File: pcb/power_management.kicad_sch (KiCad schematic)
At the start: 34 parts, among them J3 USB C, J4 BATT, Q2 AO3400A, Q3 AO3401A, SW5 POWER, U4 BQ25619, U5 AP2112K-3.3

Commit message: perf: strenghen Mahony filter (#50)
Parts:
- U5: footprint leany_footprints:TSOT-23-5 -> Package_TO_SOT_SMD:SOT-23-5
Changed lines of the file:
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@@
 (kicad_sch
-	(version 20231120)
+	(version 20250114)
 	(generator "eeschema")
-	(generator_version "8.0")
+	(generator_version "9.0")
 	(paper "A4")
 	(title_block
@@
 		(comment 2 "Copyright (c) 2023 Gilles Henrard")
 	)
+	(rectangle
+		(start 208.28 26.67)
+		(end 261.62 60.96)
+		(stroke
+			(width 0)
+			(type dash)
+		)
+		(fill
+			(type none)
+		)
+	)
+	(rectangle
+		(start 109.22 25.4)
+		(end 198.628 88.9)
+		(stroke
+			(width 0)
+			(type dash)
+		)
+		(fill
+			(type none)
+		)
+	)
+	(rectangle
+		(start 36.83 115.57)
+		(end 100.33 170.18)
+		(stroke
+			(width 0)
+			(type dash)
+		)
+		(fill
+			(type none)
+		)
+	)
+	(rectangle
+		(start 40.64 27.94)
+		(end 95.25 86.36)
+		(stroke
+			(width 0)
+			(type dash)
+		)
+		(fill
+			(type none)
+		)
+	)
+	(text "USB C connector (5V receiver)"
+		(exclude_from_sim no)
+		(at 62.484 84.836 0)
+		(effects
+			(font
+				(size 1.27 1.27)
+			)
+		)
+	)
+	(text "Battery voltage ADC measure point"
+		(exclude_from_sim no)
+		(at 55.118 165.608 0)
+		(effects
+			(font
+				(size 1.27 1.27)
+			)
+		)
+	)
+	(text "Highest input voltage regulation to 3.3V"
+		(exclude_from_sim no)
+		(at 235.458 57.15 0)
+		(effects
+			(font
+				(size 1.27 1.27)
+			)
+		)
+	)
+	(text "Avoids draining the battery when not reading its voltage"
+		(exclude_from_sim no)
+		(at 65.532 168.148 0)
+		(effects
+			(font
+				(size 1.27 1.27)
+			)
+		)
+	)
 	(junction
 		(at 166.37 53.34)
@@
 		)
 	)
-	(rectangle
-		(start 208.28 26.67)
-		(end 261.62 60.96)
-		(stroke
-			(width 0)
-			(type dash)
-		)
-		(fill
-			(type none)
-		)
-	)
-	(rectangle
-		(start 109.22 25.4)
-		(end 198.628 88.9)
-		(stroke
-			(width 0)
-			(type dash)
-		)
-		(fill
-			(type none)
-		)
-	)
-	(rectangle
-		(start 36.83 115.57)
-		(end 100.33 170.18)
-		(stroke
-			(width 0)
-			(type dash)
-		)
-		(fill
-			(type none)
-		)
-	)
-	(rectangle
-		(start 40.64 27.94)
-		(end 95.25 86.36)
-		(stroke
-			(width 0)
-			(type dash)
-		)
-		(fill
-			(type none)
-		)
-	)
-	(text "USB C connector (5V receiver)"
-		(exclude_from_sim no)
-		(at 62.484 84.836 0)
-		(effects
-			(font
-				(size 1.27 1.27)
-			)
-		)
-	)
-	(text "Battery voltage ADC measure point"
-		(exclude_from_sim no)
-		(at 55.118 165.608 0)
-		(effects
-			(font
-				(size 1.27 1.27)
-			)
-		)
-	)
-	(text "Highest input voltage regulation to 3.3V"
-		(exclude_from_sim no)
-		(at 235.458 57.15 0)
-		(effects
-			(font
-				(size 1.27 1.27)
-			)
-		)
-	)
-	(text "Avoids draining the battery when not reading its voltage"
-		(exclude_from_sim no)
-		(at 65.532 168.148 0)
-		(effects
-			(font
-				(size 1.27 1.27)
-			)
-		)
-	)
 	(global_label "BATT_VOLT"
 		(shape output)
@@
 			)
 		)
-		(property "Footprint" "leany_footprints:TSOT-23-5"
+		(property "Footprint" "Package_TO_SOT_SMD:SOT-23-5"
 			(at 237.49 31.115 0)
 			(effects

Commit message: feat: design PCB rev0.3 (#27)
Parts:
- removed J4: BATT, leany_footprints:wago_2060-452_998-404, symbol leany-symbols:wago_2060-452_998-404
- added C28: 100n, leany_footprints:C_0402_1005Metric, symbol Device:C_Small
- added J4: BATT, leany_footprints:wago_2059-302_998-403, symbol leany-symbols:wago_2059-302_998-403
- added Q4: AO3401A, Package_TO_SOT_SMD:SOT-23, symbol Transistor_FET:AO3401A
- added Q5: PT8810, Package_TO_SOT_SMD:SOT-23-6, symbol leany-symbols:PT8810
- added R25: 100R, leany_footprints:R_0402_1005Metric, symbol Device:R_Small
- added R26: 1k, leany_footprints:R_0402_1005Metric, symbol Device:R_Small
- added TP5: +BATT, leany_footprints:TestPoint_Pad_1.0x1.0mm, symbol Connector:TestPoint_Small
- added U6: DW01A, Package_TO_SOT_SMD:SOT-23-6, symbol Battery_Management:DW01A
- C14, C22, C23: footprint Capacitor_SMD:C_0603_1608Metric -> leany_footprints:C_0402_1005Metric; LCSC C15849 -> C52923
- C17, C21: footprint Capacitor_SMD:C_0603_1608Metric -> leany_footprints:C_0402_1005Metric; LCSC C14663 -> C1525
- C20: footprint Capacitor_SMD:C_0603_1608Metric -> leany_footprints:C_0402_1005Metric; LCSC C21122 -> C1532
- J3: footprint Connector_USB:USB_C_Receptacle_HRO_TYPE-C-31-M-12 -> leany_footprints:USB_C_Receptacle_HRO_TYPE-C-31-M-12
- R16, R18: footprint Resistor_SMD:R_0603_1608Metric -> leany_footprints:R_0402_1005Metric; LCSC C25804 -> C25744
- R17: footprint Resistor_SMD:R_0603_1608Metric -> leany_footprints:R_0402_1005Metric; LCSC C25803 -> C25741
- R19, R20: footprint Resistor_SMD:R_0603_1608Metric -> leany_footprints:R_0402_1005Metric; LCSC C23186 -> C25905
- R23, R24: footprint Resistor_SMD:R_0603_1608Metric -> leany_footprints:R_0402_1005Metric; LCSC C23162 -> C25900
- renumbered TP1 to TP2, TP2 to TP3, TP3 to TP4, TP4 to TP6, TP5 to TP7
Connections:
- net +BATT: now also Q4.2 (S), R25.2
- net GND: now also Q5.3 (S2), R26.1
- new net: J4.1 (1_1), J4.2 (1_2), Q4.3 (D), TP5.1
- new net: C28.1, R25.1, U6.5 (VCC)
- new net: Q5.6 (G1), U6.1 (OD)
- new net: R26.2, U6.2 (CS)
- new net: Q5.4 (G2), U6.3 (OC)
- new net: Q5.2 (S1/D2), Q5.5 (S1/D2)
- new net GNDREF: C28.2, J4.3 (2_1), J4.4 (2_2), Q4.1 (G), Q5.1 (D1), U6.6 (GND)
- no-connect marks 6 -> 7
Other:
- note added: "Battery levels and reverse-voltage protection"
- title: Leany power management -> Leany - Power management
- moved on the sheet: C19, C20, C21, C22, C23, C24, TP6, TP7, U5

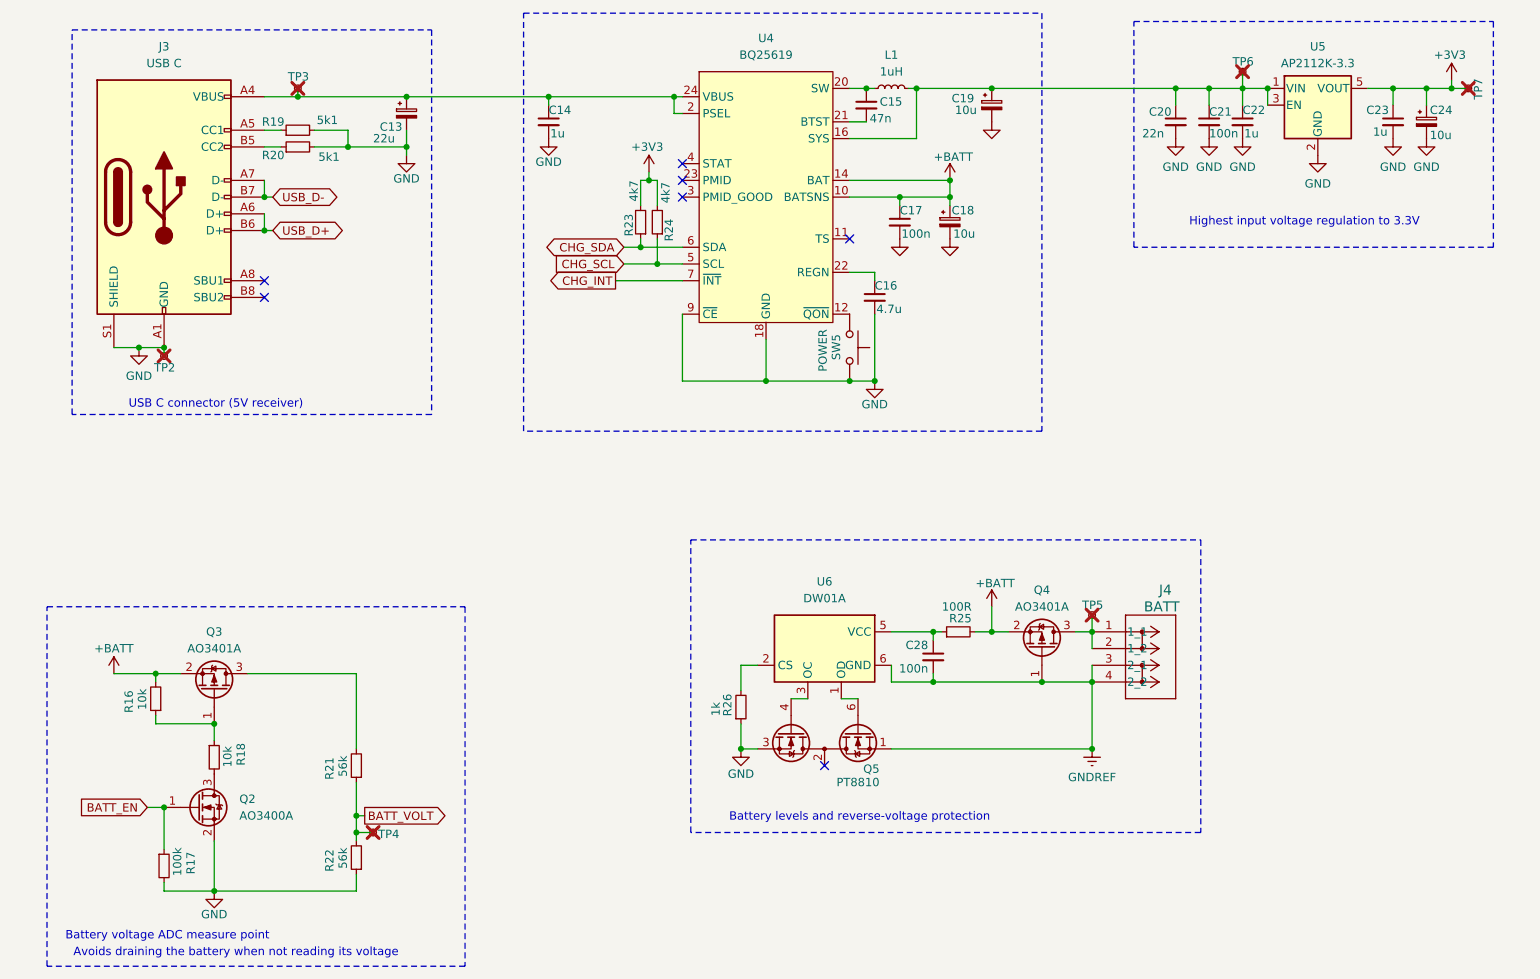
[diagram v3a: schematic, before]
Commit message: refactor: design PCB rev0.4 and fix validation workflow (#64)
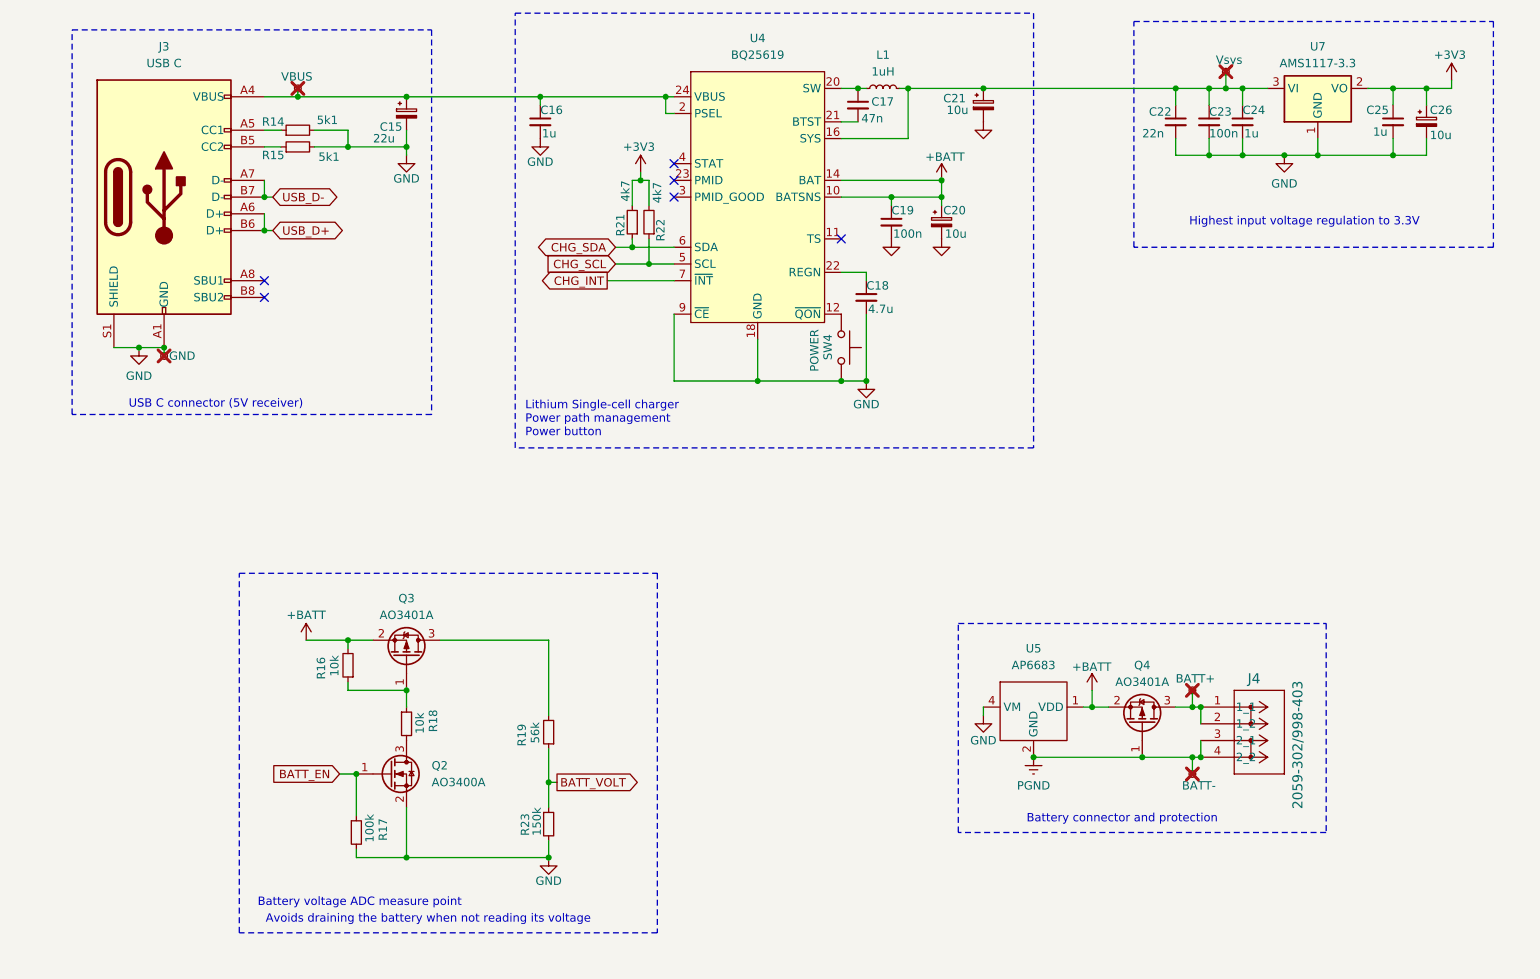
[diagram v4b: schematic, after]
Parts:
- removed C14: 1u, leany_footprints:C_0402_1005Metric, symbol Device:C_Small
- removed C15: 47n, Capacitor_SMD:C_0603_1608Metric, symbol Device:C_Small
- removed C28: 100n, leany_footprints:C_0402_1005Metric, symbol Device:C_Small
- removed Q5: PT8810, Package_TO_SOT_SMD:SOT-23-6, symbol leany-symbols:PT8810
- removed R24: 4k7, leany_footprints:R_0402_1005Metric, symbol Device:R_Small
- removed R25: 100R, leany_footprints:R_0402_1005Metric, symbol Device:R_Small
- removed R26: 1k, leany_footprints:R_0402_1005Metric, symbol Device:R_Small
- removed TP4: BATT, leany_footprints:TestPoint_Pad_1.0x1.0mm, symbol Connector:TestPoint_Small
- removed TP7: 3.3V, leany_footprints:TestPoint_Pad_1.0x1.0mm, symbol Connector:TestPoint_Small
- removed U5: AP2112K-3.3, Package_TO_SOT_SMD:SOT-23-5, symbol Regulator_Linear:AP2112K-3.3
- removed U6: DW01A, Package_TO_SOT_SMD:SOT-23-6, symbol Battery_Management:DW01A
- added C17: 47n, Capacitor_SMD:C_0603_1608Metric, symbol Device:C_Small
- added C18: 4.7u, Capacitor_SMD:C_0805_2012Metric, symbol Device:C_Small
- added R21: 4k7, leany_footprints:R_0402_1005Metric, symbol Device:R_Small
- added TP6: BATT-, leany_footprints:TestPoint_Pad_1.0x1.0mm, symbol Connector:TestPoint_Small
- added U5: AP6683, Package_DFN_QFN:UDFN-4-1EP_1x1mm_P0.65mm_EP0.48x0.48mm, symbol leany-symbols:AP6683
- added U7: AMS1117-3.3, Package_TO_SOT_SMD:SOT-223-3_TabPin2, symbol Regulator_Linear:AMS1117-3.3
- C16: value 4.7u -> 1u; footprint Capacitor_SMD:C_0805_2012Metric -> leany_footprints:C_0402_1005Metric; LCSC C1779 -> C52923
- J3: LCSC C136423 -> C2765186
- J4: value BATT -> 2059-302/998-403
- R22: value 56k -> 4k7; footprint Resistor_SMD:R_0603_1608Metric -> leany_footprints:R_0402_1005Metric; LCSC C23206 -> C25900
- R23: value 4k7 -> 150k; footprint leany_footprints:R_0402_1005Metric -> Resistor_SMD:R_0603_1608Metric; LCSC C25900 -> C22807
- TP5: value +BATT -> BATT+
- TP7: renamed from TP6; value Vin -> Vsys
- renumbered C13 to C15, C17 to C19, C18 to C20, C19 to C21, C20 to C22, C21 to C23, C22 to C24, C23 to C25, C24 to C26, R19 to R14, R20 to R15, R21 to R19, SW5 to SW4
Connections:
- net +3V3: now also R22.2, R21.2, U7.2 (VO); no longer R23.2
- net +BATT: now also U5.1 (VDD)
- net BATT_VOLT: now also R23.1; no longer R22.2
- net CHG_SCL: now also R22.1
- net CHG_SDA: now also R21.1; no longer R23.1
- net GND: now also R23.2, C18.2, U5.4 (VM), U5.5 (PAD), U7.1 (GND); no longer R22.1
- net at L1.1, U4.19 (SW), U4.20 (SW): now also C17.1
- net at C15.1, J3.A4 (VBUS), J3.A9 (VBUS)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: now also C16.1
- net at U4.21 (BTST): now also C17.2
- net at U4.22 (REGN): now also C18.1; no longer C16.1
- net GNDREF renamed PGND
- net PGND: now also TP6.1, U5.2 (GND), U5.3 (GND)
- net SYS: no longer names the net of C21.1, C22.1, C23.1, C24.1, L1.2, TP7.1, U4.15 (SYS), U4.16 (SYS)
- net SYS: now also U7.3 (VI)
- no-connect marks 7 -> 6
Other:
- note added: "Battery connector and protection"
- note added: "Lithium Single-cell charger Power path management Power button"
- note removed: "Battery levels and reverse-voltage protection"
- moved on the sheet: C19, C20, C21, L1, Q2, Q3, R16, R17, R18, R19, SW4

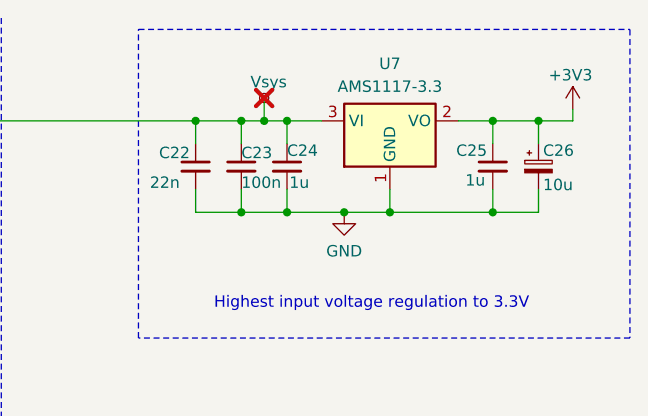
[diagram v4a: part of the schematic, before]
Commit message: fix: replace the LDO by an AP2112k-3.3 (#93)
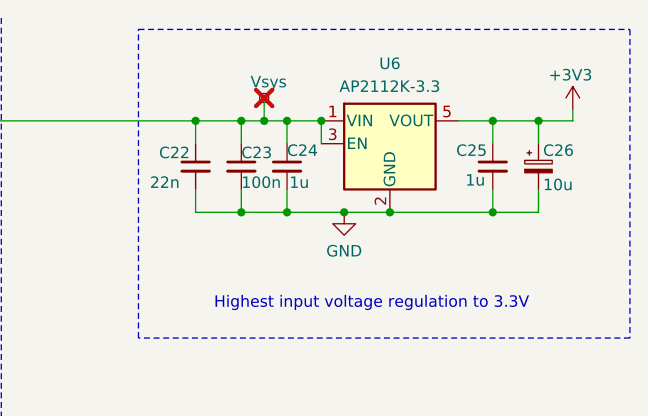
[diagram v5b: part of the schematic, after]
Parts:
- removed U7: AMS1117-3.3, Package_TO_SOT_SMD:SOT-223-3_TabPin2, symbol Regulator_Linear:AMS1117-3.3
- added U6: AP2112K-3.3, Package_TO_SOT_SMD:SOT-23-5, symbol Regulator_Linear:AP2112K-3.3
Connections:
- net +3V3: now also U6.5 (VOUT)
- net GND: now also U6.2 (GND)
- net at C21.1, C22.1, C23.1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: now also U6.1 (VIN), U6.3 (EN)
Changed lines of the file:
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@@
 	(title_block
 		(title "Leany - Power management")
-		(date "2026-02-19")
+		(date "2026-03-22")
 		(rev "0.4")
 		(comment 1 "CERN Open Hardware Licence Version 2 - Permissive")
@@
 	)
 	(junction
-		(at 229.87 46.99)
-		(diameter 0)
-		(color 0 0 0 0)
-	)
-	(junction
 		(at 172.72 53.34)
 		(diameter 0)
@@
 	)
 	(junction
+		(at 222.25 36.83)
+		(diameter 0)
+		(color 0 0 0 0)
+	)
+	(junction
 		(at 241.3 46.99)
 		(diameter 0)
@@
 	)
 	(junction
+		(at 229.87 46.99)
+		(diameter 0)
+		(color 0 0 0 0)
+	)
+	(junction
 		(at 241.3 36.83)
 		(diameter 0)
@@
 	(wire
 		(pts
+			(xy 229.87 46.99) (xy 241.3 46.99)
+		)
+		(stroke
+			(width 0)
+			(type default)
+		)
+	)
+	(wire
+		(pts
 			(xy 113.03 151.13) (xy 113.03 153.67)
 		)
@@
 	(wire
 		(pts
-			(xy 179.07 36.83) (xy 208.28 36.83)
+			(xy 222.25 39.37) (xy 222.25 36.83)
 		)
 		(stroke
@@
 	(wire
 		(pts
-			(xy 127 49.53) (xy 127 50.8)
+			(xy 179.07 36.83) (xy 208.28 36.83)
 		)
 		(stroke
@@
 	(wire
 		(pts
-			(xy 229.87 44.45) (xy 229.87 46.99)
+			(xy 127 49.53) (xy 127 50.8)
 		)
 		(stroke
@@
 	(wire
 		(pts
-			(xy 241.3 46.99) (xy 229.87 46.99)
+			(xy 224.79 46.99) (xy 229.87 46.99)
 		)
 		(stroke
@@
 	(wire
 		(pts
-			(xy 224.79 46.99) (xy 229.87 46.99)
-		)
-		(stroke
-			(width 0)
-			(type default)
-		)
-	)
-	(wire
-		(pts
 			(xy 46.99 76.2) (xy 50.8 76.2)
 		)
@@
 	)
 	(symbol
+		(lib_id "Regulator_Linear:AP2112K-3.3")
+		(at 229.87 39.37 0)
+		(unit 1)
+		(exclude_from_sim no)
+		(in_bom yes)
+		(on_board yes)
+		(dnp no)
+		(fields_autoplaced yes)
+		(property "Reference" "U6"
+			(at 229.87 30.48 0)
+			(effects
+				(font
+					(size 1.27 1.27)
+				)
+			)
+		)
+		(property "Value" "AP2112K-3.3"
+			(at 229.87 33.02 0)
+			(effects
+				(font
+					(size 1.27 1.27)
+				)
+			)
+		)
+		(property "Footprint" "Package_TO_SOT_SMD:SOT-23-5"
+			(at 229.87 31.115 0)
+			(effects
+				(font
+					(size 1.27 1.27)
+				)
+				(hide yes)
+			)
+		)
+		(property "Datasheet" "https://www.diodes.com/assets/Datasheets/AP2112.pdf"
+			(at 229.87 36.83 0)
+			(effects
+				(font
+					(size 1.27 1.27)
+				)
+				(hide yes)
+			)
+		)
+		(property "Description" "600mA low dropout linear regulator, with enable pin, 3.8V-6V input voltage range, 3.3V fixed positive output, SOT-23-5"
+			(at 229.87 39.37 0)
+			(effects
+				(font
+					(size 1.27 1.27)
+				)
+				(hide yes)
+			)
+		)
+		(property "LCSC" "C51118"
+			(at 229.87 39.37 0)
+			(effects
+				(font
+					(size 1.27 1.27)
+				)
+				(hide yes)
+			)
+		)
+		(pin "3"
+		)
+		(pin "1"
+		)
+		(pin "2"
+		)
+		(pin "4"
+		)
+		(pin "5"
+		)
+		(instances
+			(project "leany"
+				(path "/e47b2519-93ca-4a48-9414-ecc253dd35f5/702fc064-eab2-4b82-8f62-a654ccd28f72"
+					(reference "U6")
+					(unit 1)
+				)
+			)
+		)
+	)
+	(symbol
 		(lib_id "power:GND")
 		(at 165.1 59.69 0)
@@
 				)
 			)
-			(project ""
+			(project "leany"
 				(path "/e47b2519-93ca-4a48-9414-ecc253dd35f5/702fc064-eab2-4b82-8f62-a654ccd28f72"
 					(reference "Q3")
@@
 				)
 			)
-			(project ""
+			(project "leany"
 				(path "/e47b2519-93ca-4a48-9414-ecc253dd35f5/702fc064-eab2-4b82-8f62-a654ccd28f72"
 					(reference "J3")
@@
 	)
 	(symbol
-		(lib_id "Regulator_Linear:AMS1117-3.3")
-		(at 229.87 36.83 0)
-		(unit 1)
-		(exclude_from_sim no)
-		(in_bom yes)
-		(on_board yes)
-		(dnp no)
-		(fields_autoplaced yes)
-		(property "Reference" "U7"
-			(at 229.87 30.48 0)
-			(effects
-				(font
-					(size 1.27 1.27)
-				)
-			)
-		)
-		(property "Value" "AMS1117-3.3"
-			(at 229.87 33.02 0)
-			(effects
-				(font
-					(size 1.27 1.27)
-				)
-			)
-		)
-		(property "Footprint" "Package_TO_SOT_SMD:SOT-223-3_TabPin2"
-			(at 229.87 31.75 0)
-			(effects
-				(font
-					(size 1.27 1.27)
-				)
-				(hide yes)
-			)
-		)
-		(property "Datasheet" "http://www.advanced-monolithic.com/pdf/ds1117.pdf"
-			(at 232.41 43.18 0)
-			(effects
-				(font
-					(size 1.27 1.27)
-				)
-				(hide yes)
-			)
-		)
-		(property "Description" "1A Low Dropout regulator, positive, 3.3V fixed output, SOT-223"
-			(at 229.87 36.83 0)
-			(effects
-				(font
-					(size 1.27 1.27)
-				)
-				(hide yes)
-			)
-		)
-		(property "LCSC" "C6186"
-			(at 229.87 36.83 0)
-			(effects
-				(font
-					(size 1.27 1.27)
-				)
-				(hide yes)
-			)
-		)
-		(pin "1"
-		)
-		(pin "3"
-		)
-		(pin "2"
-		)
-		(instances
-			(project ""
-				(path "/e47b2519-93ca-4a48-9414-ecc253dd35f5/702fc064-eab2-4b82-8f62-a654ccd28f72"
-					(reference "U7")
-					(unit 1)
-				)
-			)
-		)
-	)
-	(symbol
 		(lib_id "Connector:TestPoint_Small")
 		(at 210.82 140.97 180)
@@
 				)
 			)
-			(project ""
+			(project "leany"
 				(path "/e47b2519-93ca-4a48-9414-ecc253dd35f5/702fc064-eab2-4b82-8f62-a654ccd28f72"
 					(reference "Q2")
